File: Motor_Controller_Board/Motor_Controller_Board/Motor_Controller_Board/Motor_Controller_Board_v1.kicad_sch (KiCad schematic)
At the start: 0 parts

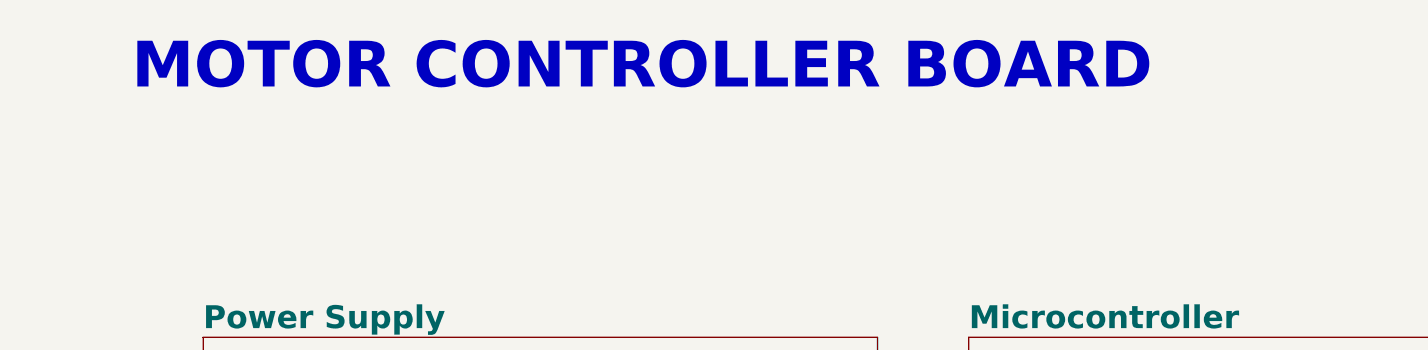
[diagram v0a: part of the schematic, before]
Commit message: discussed with Alex and Mishari. confident in schematic, going to do layout tomorrow
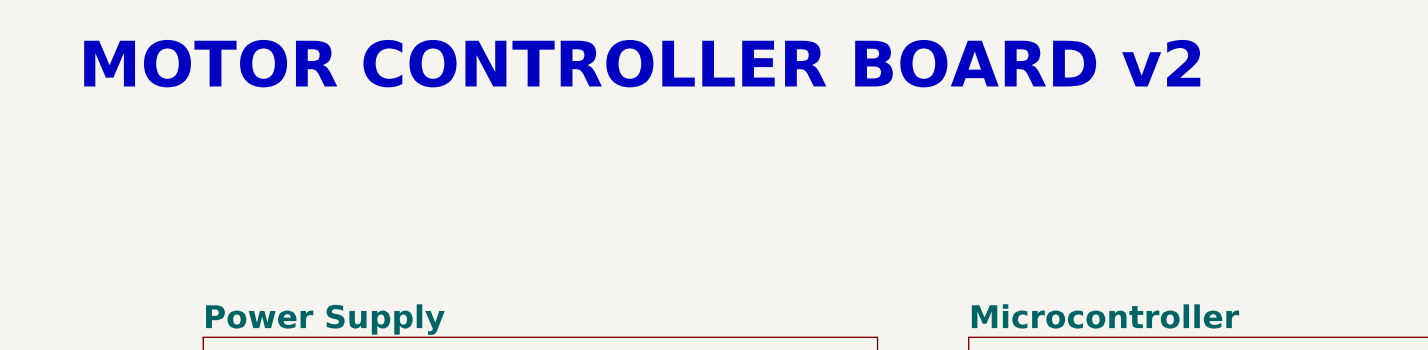
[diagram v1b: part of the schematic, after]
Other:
- note added: "MOTOR CONTROLLER BOARD v2"
- note removed: "MOTOR CONTROLLER BOARD"
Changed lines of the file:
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@@
 	(title_block
 		(title "Motor Controller Board")
+		(date "2025-05-05")
 		(rev "v1")
 		(company "University of California, Santa Cruz")
 	)
-	(text "MOTOR CONTROLLER BOARD"
+	(text "MOTOR CONTROLLER BOARD v2"
 		(exclude_from_sim no)
 		(at 66.548 18.288 0)
